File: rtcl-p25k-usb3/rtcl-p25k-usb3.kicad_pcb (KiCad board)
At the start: 2 copper layers, 60 x 32.3 mm, 56 parts, among them J1 ZX360D-B-10P(30), J2 0525592253, J3 BTB-DF40C-60DS-0.4V(51), J4 BTB-DF40C-60DS-0.4V(51), J5 JTAG, U12 TPS22917DBV, U2 TPD4E05U06DQA, U3 USBLC6-2P6, U4 FT601Q, X1 30MHz

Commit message: WIP
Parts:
- added J10: SSQ-106-02-F-D-RA, rtcl-p25k-usb3:PMOD_02x06_2.54mm, F.Cu at (176.7, 100.0)
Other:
- board size 60 x 32.3 mm -> 70 x 32.3 mm

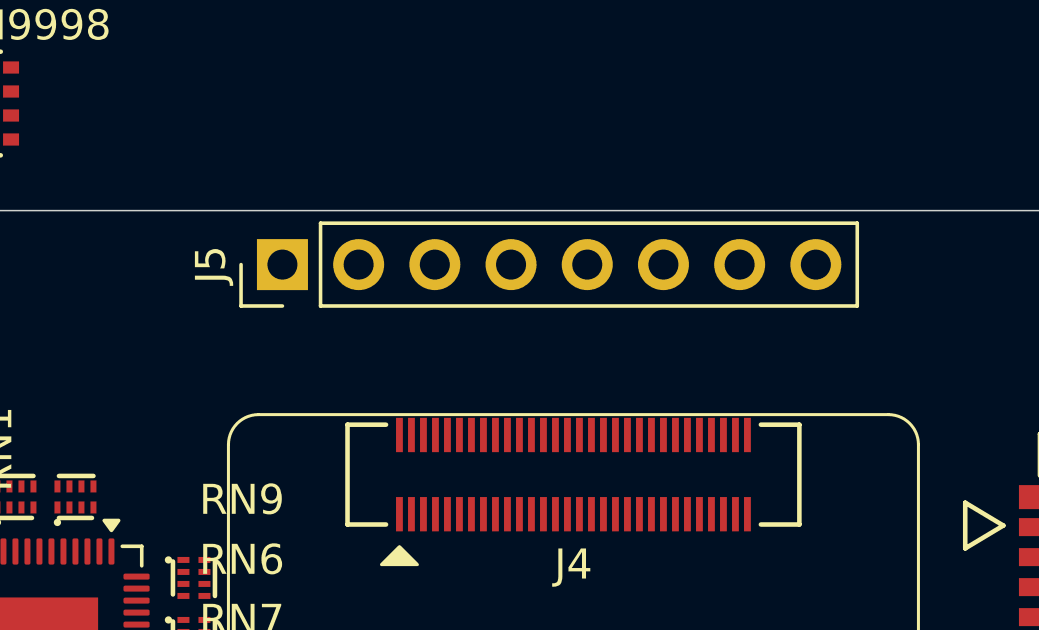
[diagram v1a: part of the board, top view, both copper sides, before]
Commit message: Update KiCad project files for rtcl-p25k-usb3
- Changed active layer from 25 to 5 in the project file.
- Updated footprint property for components in the schematic:
  - Changed footprint for a connector to "rtcl-p25k-usb3:CON_525592253_MOL".
  - Updated value for a component from "BTB-DF40C-60DS-0.4V(51)" to "DF40C-60DS-0.4V(51)".
  - Changed footprint for another component to "rtcl-p25k-usb3:PMOD_02x06_2.54mm".
- Modified UUIDs for various graphical elements in the CONN_DF40C-60DS_HIR module.
- Added a 3D model reference for the DF40C-60DS-0.4V(51) component.
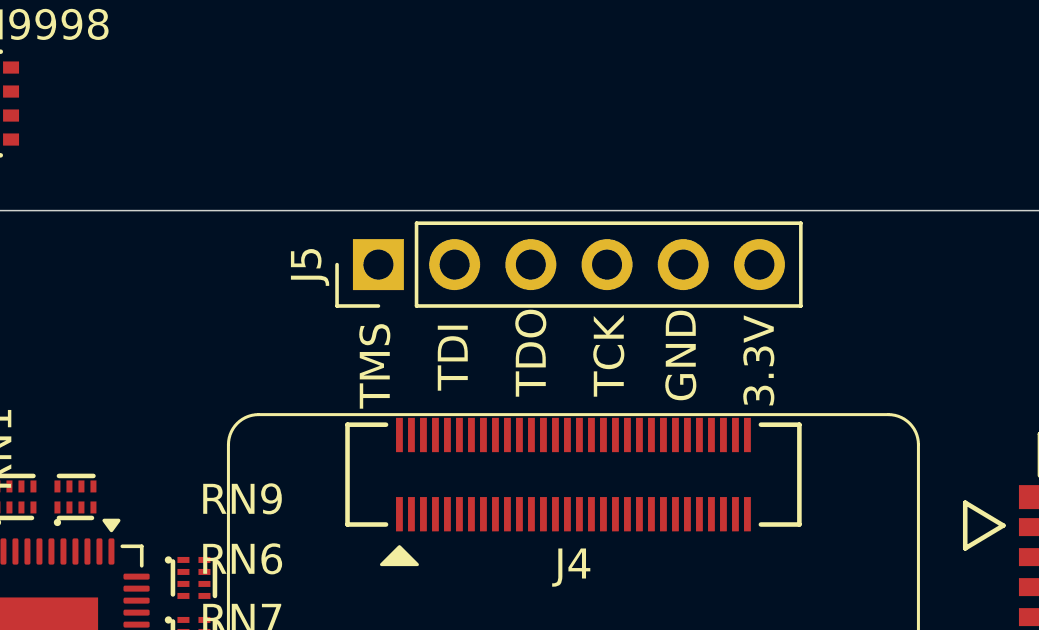
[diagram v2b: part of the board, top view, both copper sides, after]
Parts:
- J4: value BTB-DF40C-60DS-0.4V(51) -> DF40C-60DS-0.4V(51)
- J5: footprint Connector_PinHeader_2.54mm:PinHeader_1x08_P2.54mm_Vertical -> Connector_PinHeader_2.54mm:PinHeader_1x06_P2.54mm_Vertical
- moved J5 3.20 mm to (143.5, 86.0)
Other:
- board text added: "3.3V"
- board text added: "GND"
- board text added: "TCK"
- board text added: "TDI"
- board text added: "TDO"
- board text added: "TMS"
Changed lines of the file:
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@@
 		)
 	)
-	(footprint "Connector_PinHeader_2.54mm:PinHeader_1x08_P2.54mm_Vertical"
+	(footprint "Connector_PinHeader_2.54mm:PinHeader_1x06_P2.54mm_Vertical"
 		(layer "F.Cu")
-		(at 140.3 86 90)
-		(descr "Through hole straight pin header, 1x08, 2.54mm pitch, single row")
-		(tags "Through hole pin header THT 1x08 2.54mm single row")
+		(at 143.5 86 90)
+		(descr "Through hole straight pin header, 1x06, 2.54mm pitch, single row")
+		(tags "Through hole pin header THT 1x06 2.54mm single row")
 		(property "Reference" "J5"
 			(at 0 -2.38 90)
@@
 		)
 		(property "Value" "JTAG"
-			(at 0 20.16 90)
+			(at 0 15.08 90)
 			(layer "F.Fab")
 			(effects
@@
 		(fp_line
 			(start 1.38 1.27)
-			(end 1.38 19.16)
+			(end 1.38 14.08)
 			(stroke
 				(width 0.12)
@@
 		(fp_line
 			(start -1.38 1.27)
-			(end -1.38 19.16)
+			(end -1.38 14.08)
 			(stroke
 				(width 0.12)
@@
 		)
 		(fp_line
-			(start -1.38 19.16)
-			(end 1.38 19.16)
+			(start -1.38 14.08)
+			(end 1.38 14.08)
 			(stroke
 				(width 0.12)
@@
 		(fp_rect
 			(start -1.77 -1.77)
-			(end 1.77 19.55)
+			(end 1.77 14.47)
 			(stroke
 				(width 0.05)
@@
 		(fp_line
 			(start 1.27 -1.27)
-			(end 1.27 19.05)
+			(end 1.27 13.97)
 			(stroke
 				(width 0.1)
@@
 		)
 		(fp_line
-			(start 1.27 19.05)
-			(end -1.27 19.05)
+			(start 1.27 13.97)
+			(end -1.27 13.97)
 			(stroke
 				(width 0.1)
@@
 		)
 		(fp_line
-			(start -1.27 19.05)
+			(start -1.27 13.97)
 			(end -1.27 -0.635)
 			(stroke
@@
 		)
 		(fp_text user "${REFERENCE}"
-			(at 0 8.89 0)
+			(at 0 6.35 180)
 			(layer "F.Fab")
 			(effects
@@
 			(pintype "passive")
 		)
-		(pad "7" thru_hole circle
-			(at 0 15.24 90)
-			(size 1.7 1.7)
-			(drill 1)
-			(layers "*.Cu" "*.Mask")
-			(remove_unused_layers no)
-		)
-		(pad "8" thru_hole circle
-			(at 0 17.78 90)
-			(size 1.7 1.7)
-			(drill 1)
-			(layers "*.Cu" "*.Mask")
-			(remove_unused_layers no)
-		)
 		(embedded_fonts no)
-		(model "${KICAD10_3DMODEL_DIR}/Connector_PinHeader_2.54mm.3dshapes/PinHeader_1x08_P2.54mm_Vertical.step"
+		(model "${KICAD10_3DMODEL_DIR}/Connector_PinHeader_2.54mm.3dshapes/PinHeader_1x06_P2.54mm_Vertical.step"
 			(offset
 				(xyz 0 0 0)
@@
 		)
 		(embedded_fonts no)
+		(model "C:/Users/ryuji/OneDrive/Documents/Development/kicad/rtcl-p25k-usb3/datasheet/model/DF40C-60DS-0.4V(51)_CL0684-4004-6-51_3DDrawing_STEP_0001218420S/DF40C-60DS.stp"
+			(offset
+				(xyz 2.1 0 0)
+			)
+			(scale
+				(xyz 1 1 1)
+			)
+			(rotate
+				(xyz -90 -0 -90)
+			)
+		)
 	)
 	(footprint "Package_SON:USON-10_2.5x1.0mm_P0.5mm"
@@
 		(sheetname "/")
 		(sheetfile "rtcl-p25k-usb3.kicad_sch")
+		(units
+			(unit
+				(name "A")
+				(pins "1" "3" "5" "7" "9" "11" "2" "4" "6" "8" "10" "12")
+			)
+		)
 		(attr through_hole)
 		(duplicate_pad_numbers_are_jumpers no)
@@
 		(sheetname "/")
 		(sheetfile "rtcl-p25k-usb3.kicad_sch")
+		(units
+			(unit
+				(name "A")
+				(pins "1" "2" "3" "4" "5" "6" "7" "8" "9" "10" "11" "12" "13" "14" "15"
+					"16" "17" "18" "19" "20" "21" "22"
+				)
+			)
+		)
 		(attr smd)
 		(duplicate_pad_numbers_are_jumpers no)
@@
 		(sheetname "/")
 		(sheetfile "rtcl-p25k-usb3.kicad_sch")
+		(units
+			(unit
+				(name "A")
+				(pins "SH" "8" "5" "1" "2" "3" "4" "6" "7" "9" "10")
+			)
+		)
 		(attr smd)
 		(duplicate_pad_numbers_are_jumpers no)
@@
 			)
 		)
-		(property "Value" "BTB-DF40C-60DS-0.4V(51)"
+		(property "Value" "DF40C-60DS-0.4V(51)"
 			(at -1.200003 5.68 0)
 			(unlocked yes)
@@
 		)
 		(embedded_fonts no)
+		(model "C:/Users/ryuji/OneDrive/Documents/Development/kicad/rtcl-p25k-usb3/datasheet/model/DF40C-60DS-0.4V(51)_CL0684-4004-6-51_3DDrawing_STEP_0001218420S/DF40C-60DS.stp"
+			(offset
+				(xyz 2.1 0 0)
+			)
+			(scale
+				(xyz 1 1 1)
+			)
+			(rotate
+				(xyz -90 -0 -90)
+			)
+		)
 	)
 	(footprint "Capacitor_SMD:C_0402_1005Metric"
@@
 		(layer "User.1")
 	)
+	(gr_text "TMS"
+		(at 144 90.8 90)
+		(layer "F.SilkS")
+		(effects
+			(font
+				(size 1 1)
+				(thickness 0.15)
+			)
+			(justify left bottom)
+		)
+	)
+	(gr_text "TDI"
+		(at 146.6 90.2 90)
+		(layer "F.SilkS")
+		(effects
+			(font
+				(size 1 1)
+				(thickness 0.15)
+			)
+			(justify left bottom)
+		)
+	)
+	(gr_text "TDO"
+		(at 149.2 90.4 90)
+		(layer "F.SilkS")
+		(effects
+			(font
+				(size 1 1)
+				(thickness 0.15)
+			)
+			(justify left bottom)
+		)
+	)
+	(gr_text "TCK"
+		(at 151.8 90.4 90)
+		(layer "F.SilkS")
+		(effects
+			(font
+				(size 1 1)
+				(thickness 0.15)
+			)
+			(justify left bottom)
+		)
+	)
+	(gr_text "GND"
+		(at 154.2 90.6 90)
+		(layer "F.SilkS")
+		(effects
+			(font
+				(size 1 1)
+				(thickness 0.15)
+			)
+			(justify left bottom)
+		)
+	)
+	(gr_text "3.3V"
+		(at 156.8 90.8 90)
+		(layer "F.SilkS")
+		(effects
+			(font
+				(size 1 1)
+				(thickness 0.15)
+			)
+			(justify left bottom)
+		)
+	)
 	(embedded_fonts no)

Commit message: WIP
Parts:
- added C16: 0.1uF, Capacitor_SMD:C_0402_1005Metric, F.Cu at (137.2, 99.8)
- added C17: 0.1uF, Capacitor_SMD:C_0402_1005Metric, F.Cu at (85.9, 144.1)
- added C18: 0.1uF, Capacitor_SMD:C_0402_1005Metric, F.Cu at (85.9, 146.0)
- added C19: 0.1uF, Capacitor_SMD:C_0402_1005Metric, F.Cu at (85.9, 148.0)
- added C20: 0.1uF, Capacitor_SMD:C_0402_1005Metric, F.Cu at (85.9, 150.0)
- moved C7 71.3 mm to (131.4, 106.2), turned to 90 degrees
- moved R43 10.0 mm to (137.4, 104.6)
- moved RN2 0.90 mm to (127.8, 106.2)
- moved RN3 0.90 mm to (129.8, 106.2)
- moved RN7 0.76 mm to (137.3, 101.2)
- moved RN8 0.76 mm to (137.3, 103.2)
- moved RN6 0.21 mm to (137.2, 98.3)
- moved RN9 0.21 mm to (137.2, 96.3)
- renumbered U4 to U1

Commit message: Refactor code structure for improved readability and maintainability
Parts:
- removed RN10, RN11: YC104-JR-0722RL, rtcl-p25k-usb3:RES_YC104_YAG
- added R44: 22, Resistor_SMD:R_0402_1005Metric, F.Cu at (131.9, 93.7)
- added R45: 22, Resistor_SMD:R_0402_1005Metric, F.Cu at (130.9, 93.7)
- added R46: 22, Resistor_SMD:R_0402_1005Metric, F.Cu at (128.6, 93.7)
- added R47: 22, Resistor_SMD:R_0402_1005Metric, F.Cu at (127.6, 93.7)
- moved C20 67.8 mm to (125.6, 95.0), turned to -90 degrees
- moved C17 66.8 mm to (129.9, 93.7), turned to -90 degrees
- moved C18 66.4 mm to (137.4, 104.1), turned to 180 degrees
- moved C19 63.6 mm to (125.2, 97.9), turned to 90 degrees
- moved C10 63.2 mm to (124.8, 103.5)
- moved C8 63.1 mm to (124.9, 99.8)
- moved C9 61.3 mm to (124.8, 104.5)
- moved RN8 0.50 mm to (137.4, 102.7)
- moved R43 0.50 mm to (137.4, 105.1)
- moved C16 0.45 mm to (137.4, 99.4)
- moved RN7 0.40 mm to (137.4, 100.8)
- moved RN6 0.36 mm to (137.4, 98.0)
- moved RN9 0.28 mm to (137.4, 96.1)
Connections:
- net /G7_IOT68B renamed /G8_IOT68B
- net /MIPI3_SCK renamed /MIPI_SCL
- net /MIPI3_SDA renamed /MIPI_SDA
- J2 pad 17: /B3_IOB56A_UART_RX -> /MIPI_GPIO0
- J2 pad 18: /C3_IOB56B_UART_TX -> /MIPI_GPIO1
- J3 pad 23: /B3_IOB56A_UART_RX -> /E3_IOB60A_40P
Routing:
- net /E1_IOB12B_40P: track 0.00 -> 2.96 mm
- net /A3_JTAG_TDI: track 0.00 -> 2.24 mm
- net /D1_IOB14B_40P: track 0.00 -> 1.02 mm
- net /D7_DONE: track 0.00 -> 0.92 mm
- net /C3_IOB56B_UART_TX: track 0.00 -> 0.92 mm
- net /B3_IOB56A_UART_RX: track 0.00 -> 0.92 mm
- net /B2_IOB4A_40P: track 0.00 -> 0.92 mm
- net /E8_READY: track 0.00 -> 0.92 mm
- net /E3_IOB60A_40P: track 0.00 -> 0.92 mm
